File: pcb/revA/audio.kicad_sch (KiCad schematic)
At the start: 43 parts, among them J3 PJ307, J4 Conn_01x04, U10 PCM5102A, U11 PCM1808PWR, U8 YMF262-M, U9 SAM2695

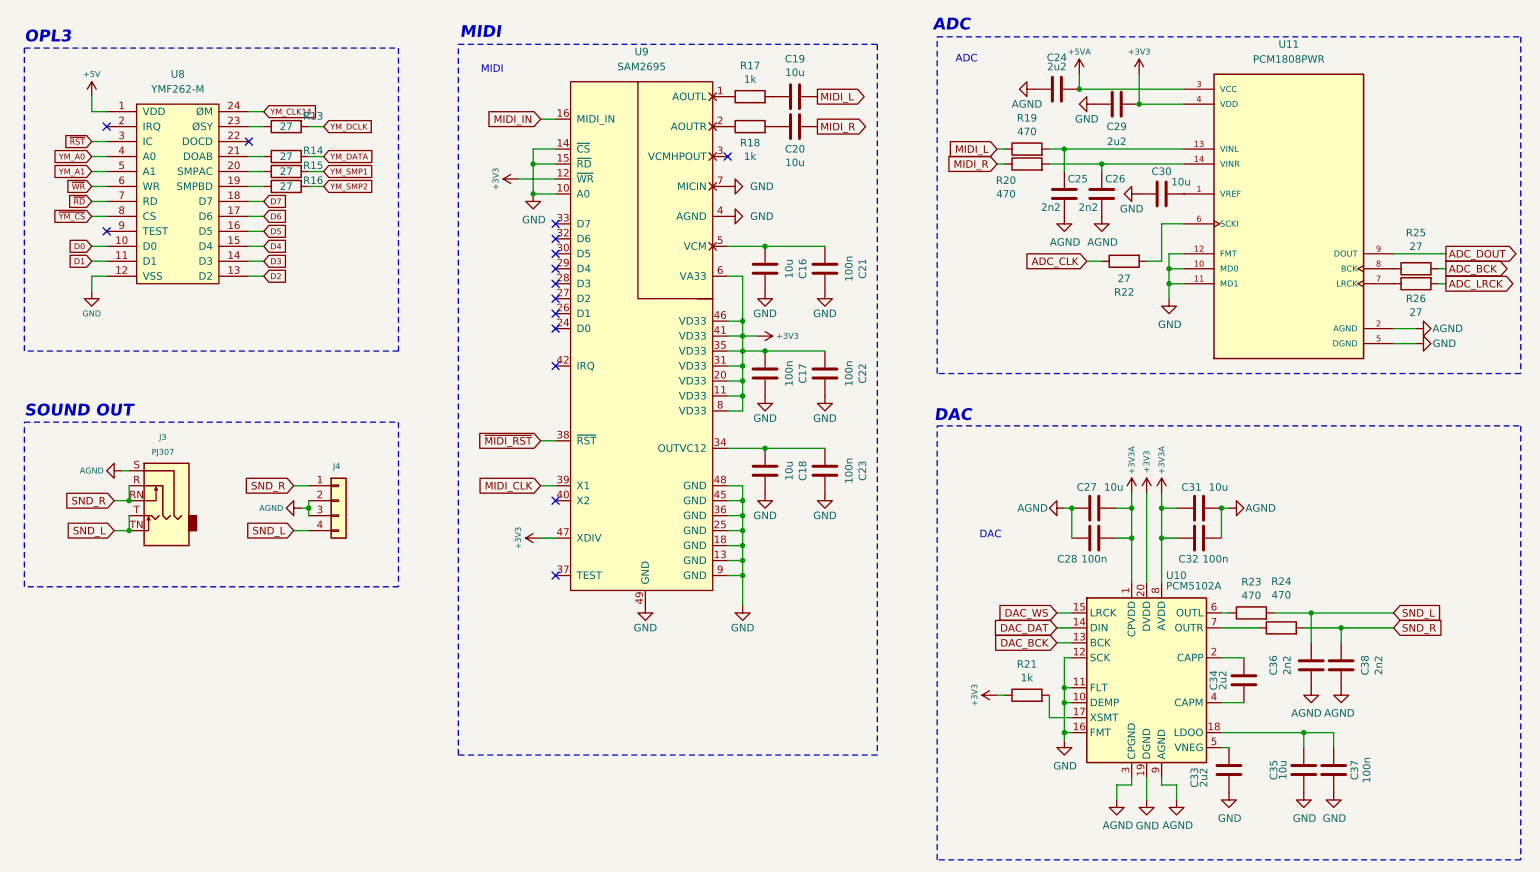
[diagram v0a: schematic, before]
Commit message: Updated gerbers to min 0.2/0.45 vias, firmware build for xc6slx16
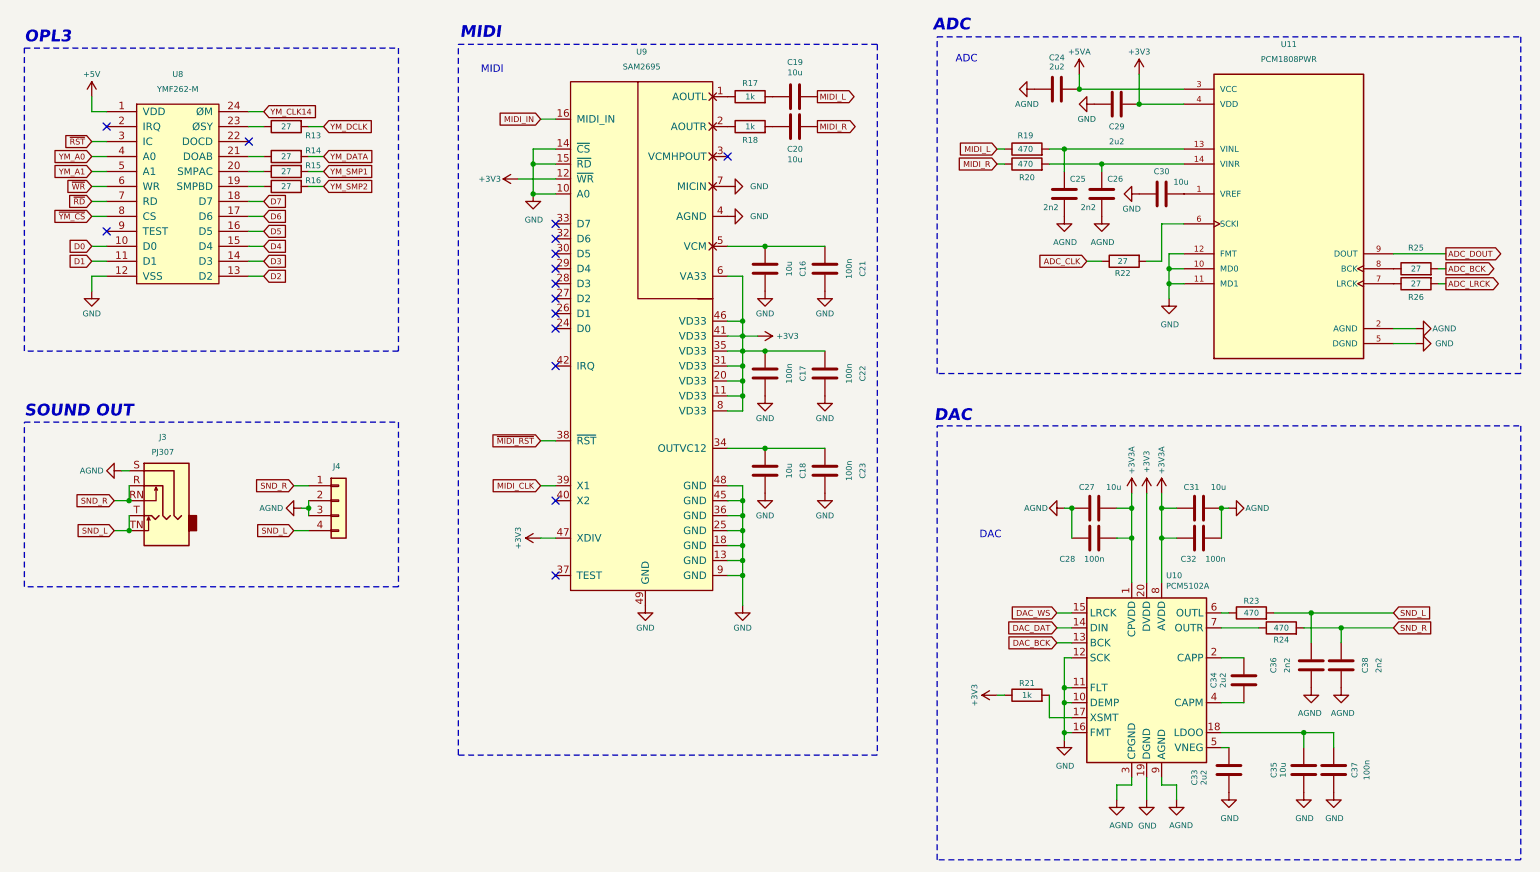
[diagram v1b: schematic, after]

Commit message: WIP
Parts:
- U11: footprint footprints:SOP65P640X120-14N -> Package_SO:TSSOP-14_4.4x5mm_P0.65mm
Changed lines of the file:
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@@
 			)
 		)
-		(property "Footprint" "footprints:SOP65P640X120-14N"
+		(property "Footprint" "Package_SO:TSSOP-14_4.4x5mm_P0.65mm"
 			(at 238.76 49.53 0)
 			(hide yes)

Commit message: Updated revA - rerouted OPL3 reset to /MIDI_RST
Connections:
- net ~{RST} is gone; now on net ~{MIDI_RST}: U8.3 (IC)
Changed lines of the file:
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@@
 	(title_block
 		(title "Karabas-MegaBuzz")
-		(date "2026-04-18")
+		(date "2026-06-03")
 		(rev "A")
 		(company "Andy Karpov")
@@
 		)
 	)
-	(global_label "~{RST}"
+	(global_label "~{MIDI_RST}"
 		(shape input)
 		(at 35.56 38.1 180)
@@
 		)
 		(property "Intersheetrefs" "${INTERSHEET_REFS}"
-			(at 30.4688 38.1 0)
+			(at 26.648 38.1 0)
 			(hide yes)
 			(show_name no)

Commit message: Updated revA (cosmetic changes)
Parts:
- J4: now not fitted; now left out of the parts list
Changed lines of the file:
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@@
 		(body_style 1)
 		(exclude_from_sim no)
-		(in_bom yes)
+		(in_bom no)
 		(on_board yes)
 		(in_pos_files yes)
-		(dnp no)
+		(dnp yes)
 		(property "Reference" "J4"
 			(at 76.5048 93.218 0)
